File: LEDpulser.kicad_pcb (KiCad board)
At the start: 2 copper layers, 50.7 x 77.8 mm, 70 parts, among them J1 RJHSE-5380, J2 EPS.00.250.NTN, J3 EPS.00.250.NTN, J4 EB21A-04-D, J5 EPL.0S.302.HLN, Q1 BVSS84LT1G, Q2 DMN3028LQ-7, Q3 DMN3028LQ-7, SW1 BST11T2AVR, U1 74AHCT123APW,118, U10 LT3082EST#TRPBF, U2 74AHCT123APW,118, U3 74AHCT123APW,118, U4 SN74LVC2G74, U5 LT1121CST-5#TRPBF, U6 IXDI602SIATR, U7 NE555S-13, U8 PM8834, U9 PM8834

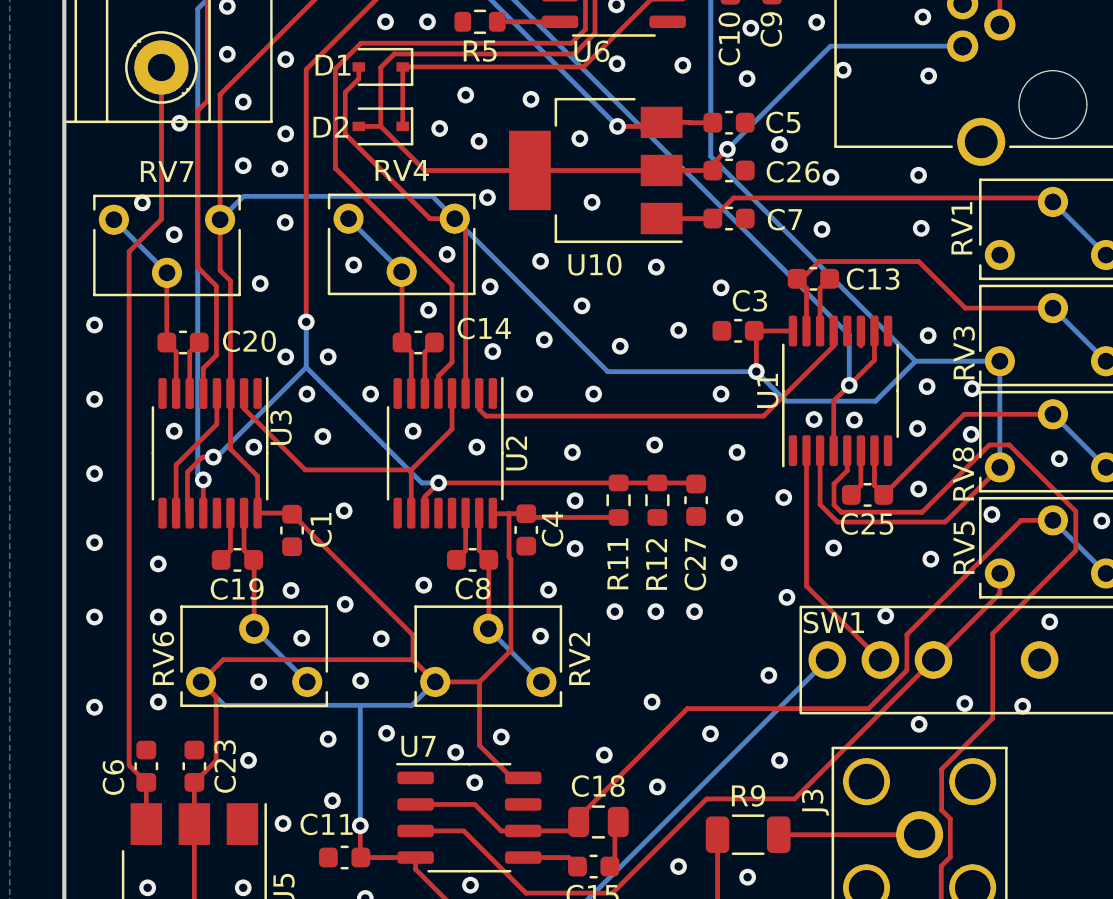
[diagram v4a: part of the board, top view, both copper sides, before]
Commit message: Fixed enable for sync pulse monostable
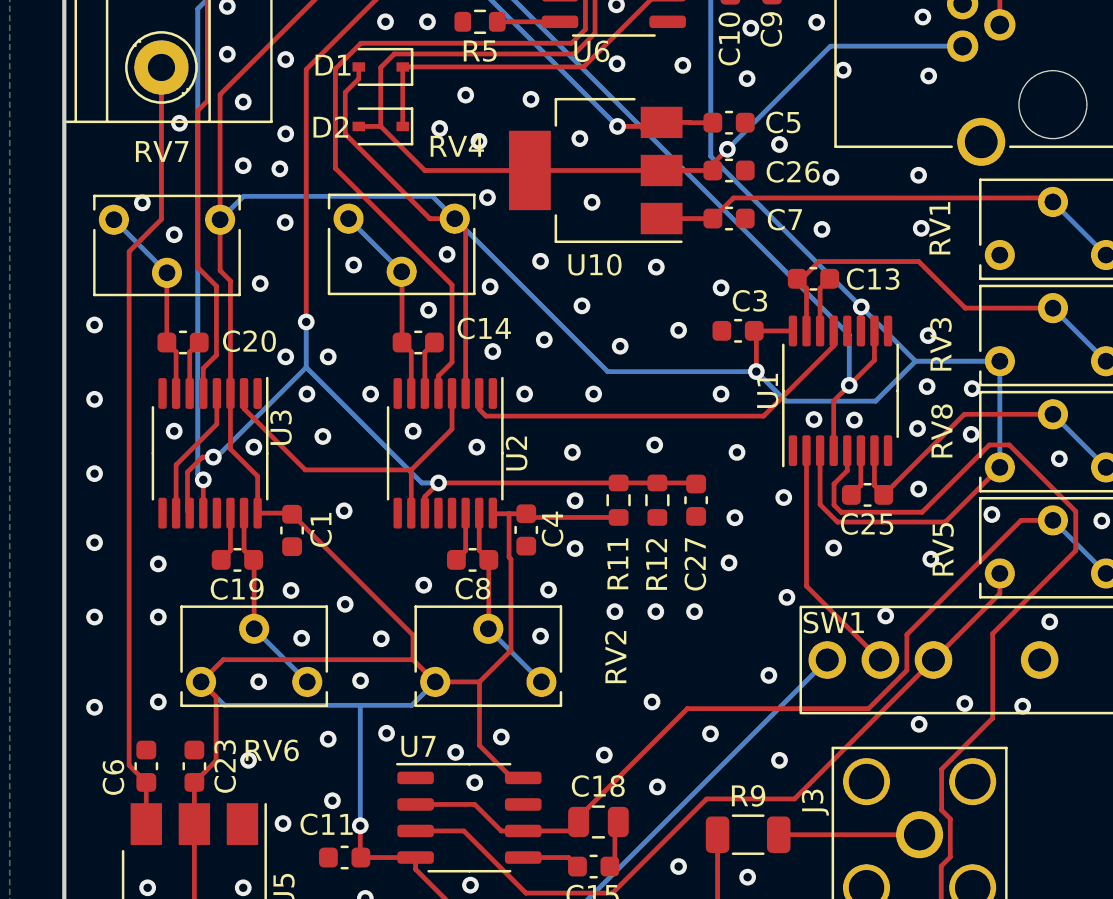
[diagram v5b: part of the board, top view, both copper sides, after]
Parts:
- U5: value LT1121CST-5#TRPBF -> LT1117
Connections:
- U1 pad 11: GND -> VCC
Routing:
- net VCC: track 253.2 -> 254.3 mm, vias 3 -> 4
- net GND: track 24.3 -> 23.6 mm

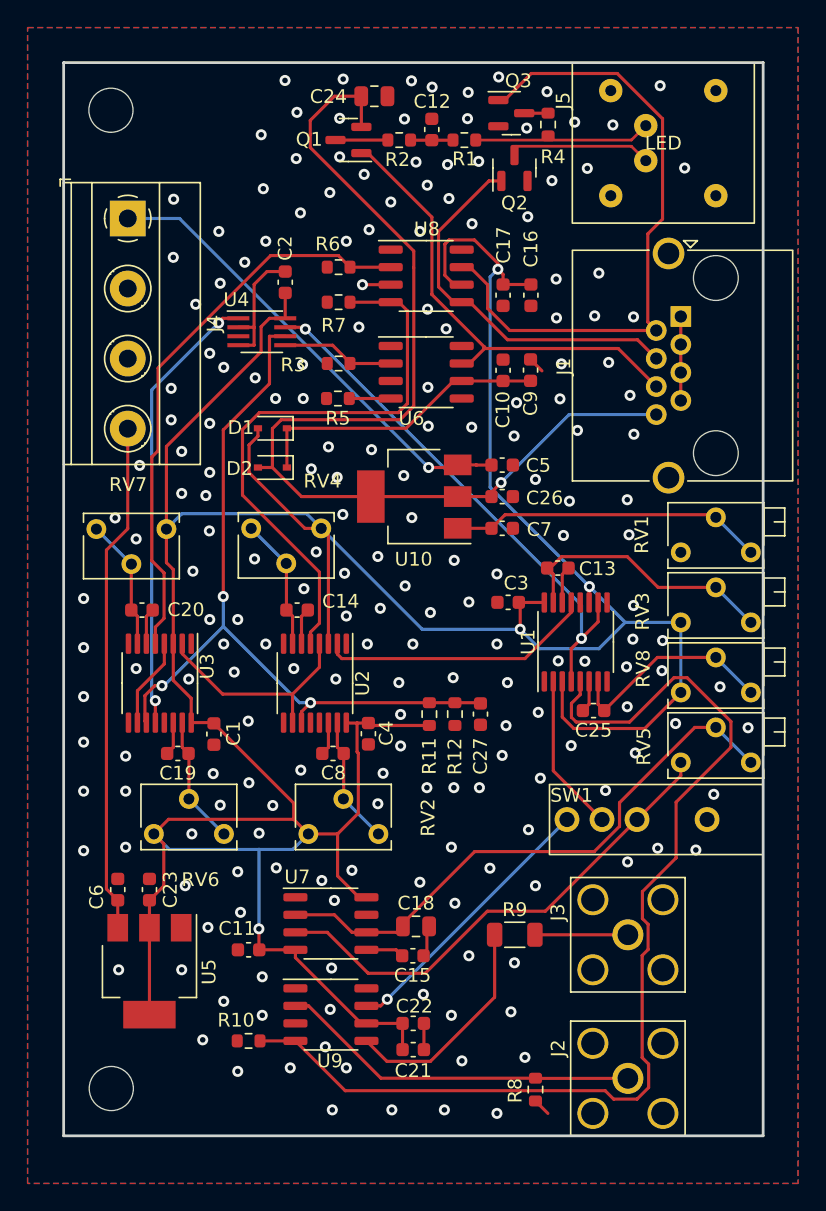
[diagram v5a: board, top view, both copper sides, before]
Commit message: Added third mounting hole. Added cutout for LEMO-connector back-side nuts.
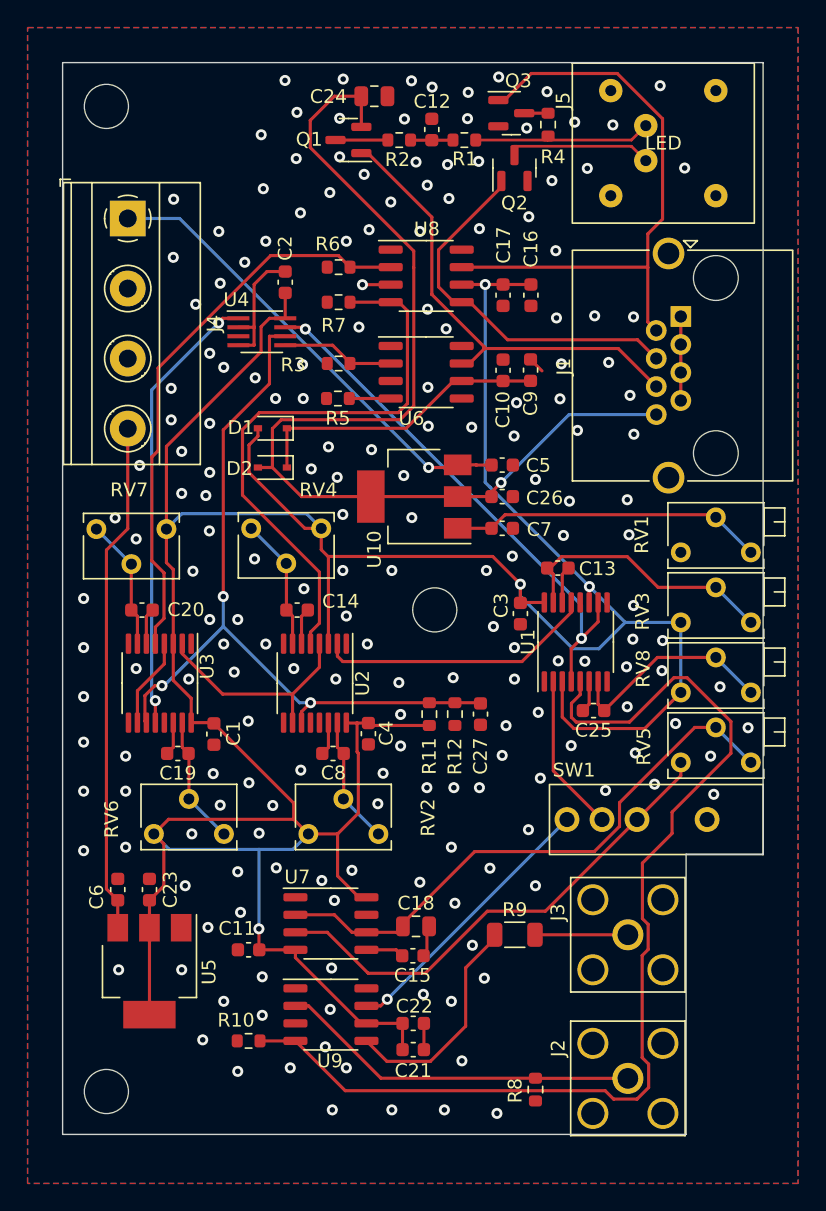
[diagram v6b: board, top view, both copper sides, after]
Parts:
- added H3: MountingHole, MountingHole:MountingHole_3.2mm_M3, F.Cu at (115.9, 65.1)
- moved C3 1.20 mm to (122.1, 65.4), turned to -90 degrees
- moved H1 0.43 mm to (92.1, 28.6)
- moved H2 0.42 mm to (92.1, 100.0)
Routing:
- net VCC: track 254.3 -> 245.2 mm
- net /LED_SHORT_OUT: track 46.1 -> 43.2 mm
- net GND: track 23.6 -> 22.3 mm, vias 203 -> 194
- net /LED_ON_OUT: track 26.9 -> 26.4 mm
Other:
- board size 50.7 x 77.8 mm -> 50.8 x 77.7 mm

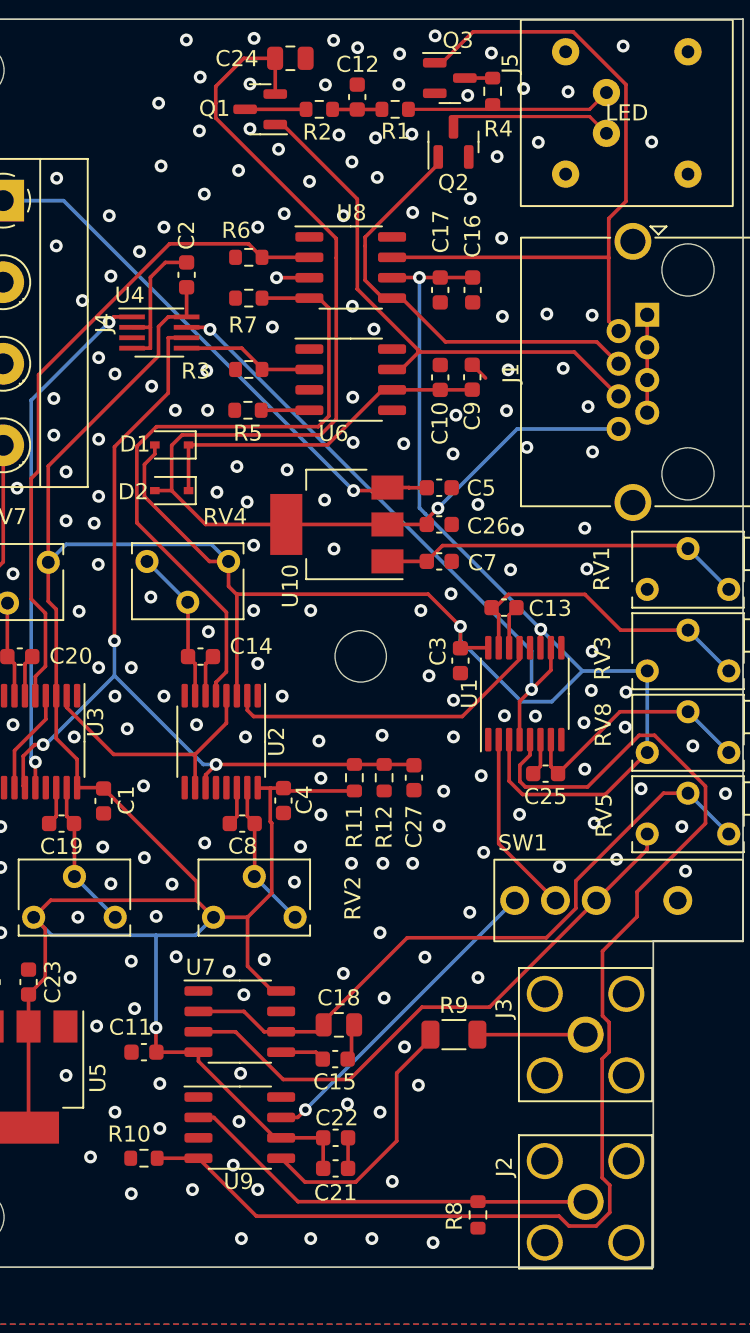
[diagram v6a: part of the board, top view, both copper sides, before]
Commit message: Added labeling to back silk screen
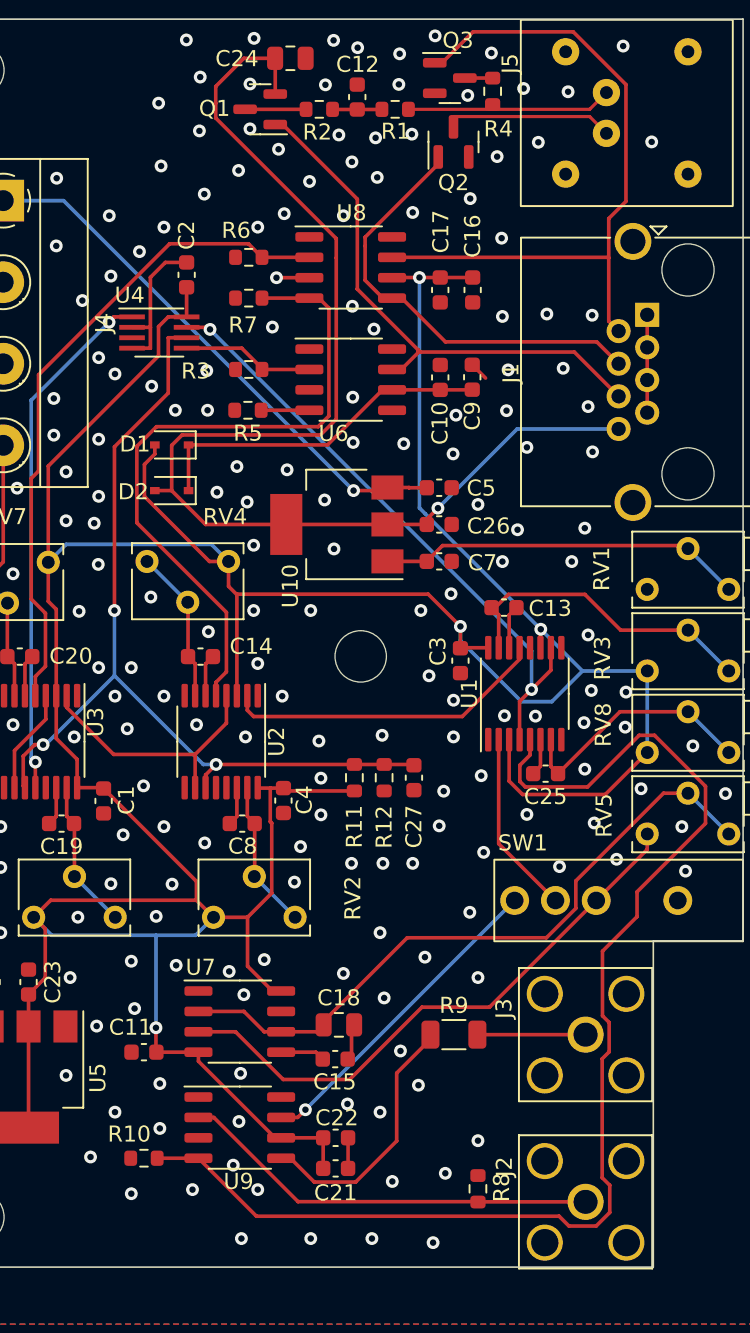
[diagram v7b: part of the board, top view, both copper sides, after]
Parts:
- moved R8 1.63 mm to (123.2, 98.2), turned to 90 degrees
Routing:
- net GND: vias 194 -> 196
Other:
- board text added: "+24V"
- board text added: "+6V"
- board text added: "C12 Charge"
- board text added: "External"
- board text added: "External Trigger In"
- board text added: "GND"
- board text added: "Internal"
- board text added: "LED On"
- board text added: "LED On Delay"
- board text added: "LED On Width"
- board text added: "LED Pulser v2"
- board text added: "LED Short"
- board text added: "LED Short Delay"
- board text added: "LED Short Width"
- board text added: "LED Voltage"
- board text added: "Sync Delay"
- board text added: "Sync Out"
- board text added: "Sync Width"
- board text added: "Trigger Rate Internal"

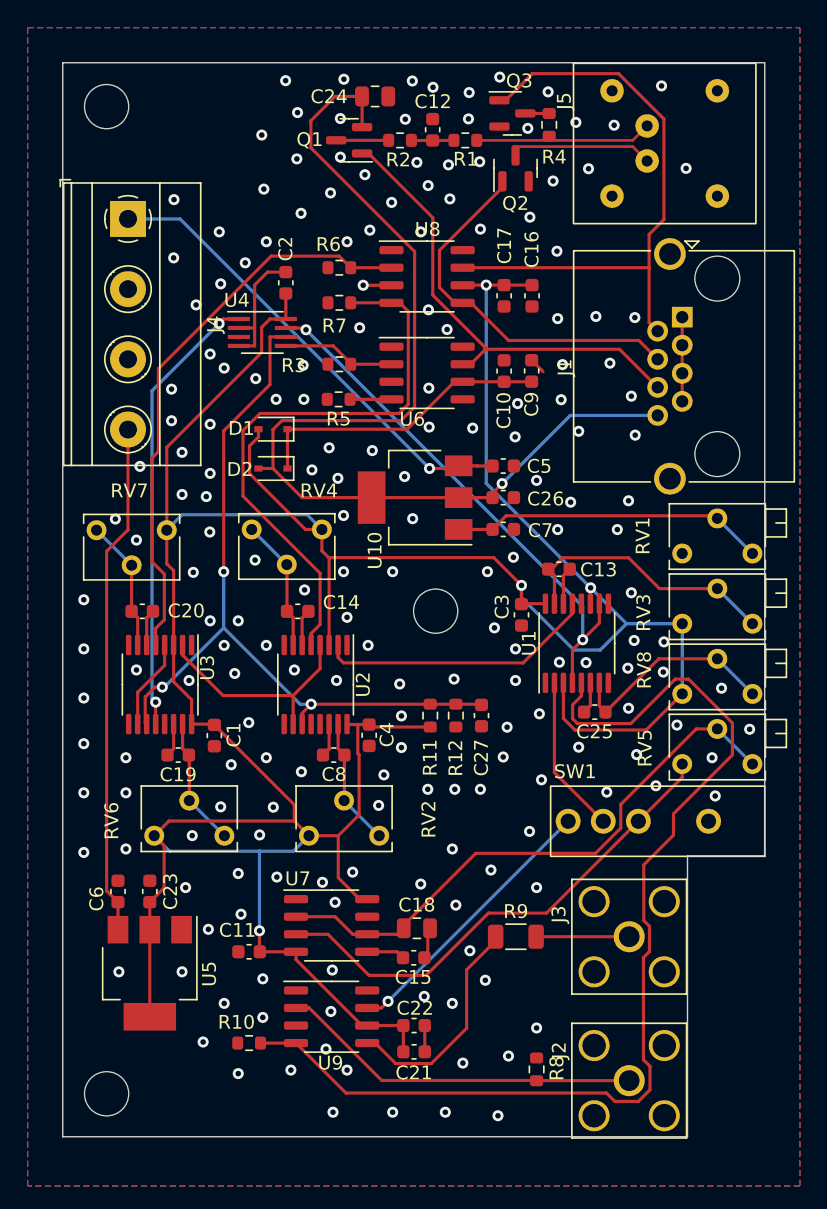
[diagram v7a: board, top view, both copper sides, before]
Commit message: Added series resistors for pots.
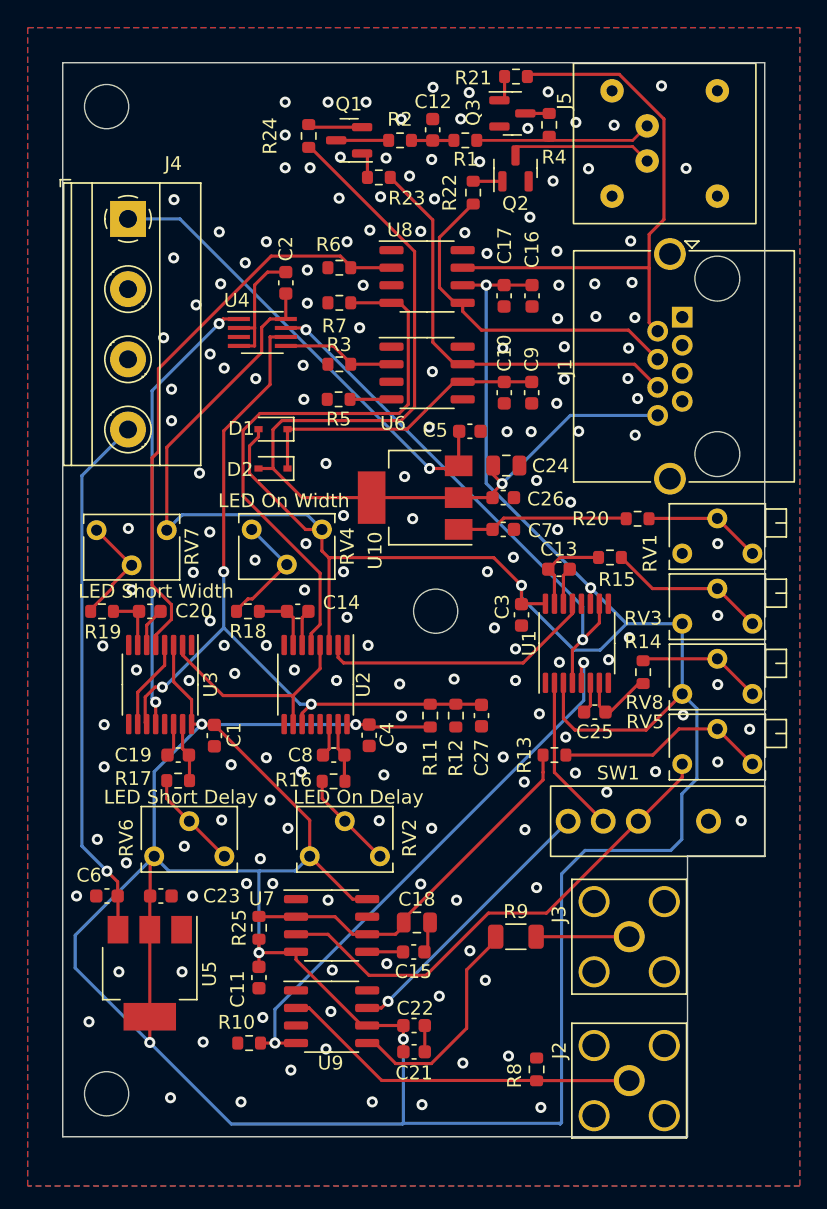
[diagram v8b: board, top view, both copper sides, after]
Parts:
- added R13: 22, Resistor_SMD:R_0603_1608Metric, F.Cu at (124.5, 75.5)
- added R14: 0, Resistor_SMD:R_0603_1608Metric, F.Cu at (130.9, 69.5)
- added R15: 0, Resistor_SMD:R_0603_1608Metric, F.Cu at (128.5, 61.2)
- added R16: 0, Resistor_SMD:R_0603_1608Metric, F.Cu at (108.5, 77.4)
- added R17: 0, Resistor_SMD:R_0603_1608Metric, F.Cu at (97.2, 77.3)
- added R18: 0, Resistor_SMD:R_0603_1608Metric, F.Cu at (102.3, 65.1)
- added R19: 0, Resistor_SMD:R_0603_1608Metric, F.Cu at (91.7, 65.1)
- added R20: 0, Resistor_SMD:R_0603_1608Metric, F.Cu at (130.5, 58.4)
- added R21: 0, Resistor_SMD:R_0603_1608Metric, F.Cu at (121.7, 26.4)
- added R22: 0, Resistor_SMD:R_0603_1608Metric, F.Cu at (118.6, 34.8)
- added R23: 0, Resistor_SMD:R_0603_1608Metric, F.Cu at (111.8, 33.7)
- added R24: 0, Resistor_SMD:R_0603_1608Metric, F.Cu at (106.7, 30.7)
- added R25: DNP, Resistor_SMD:R_0603_1608Metric, F.Cu at (103.1, 88.0)
- Q1: value BVSS84LT1G -> DMP32D4S
- R2: value 1k -> 10k
- RV1: value 2k -> 2Meg
- RV2, RV3: value 500 -> 2k
- moved C24 28.3 mm to (121.0, 54.5)
- moved C5 3.49 mm to (118.4, 52.1)
- moved C11 1.99 mm to (103.1, 91.6), turned to -90 degrees
- moved C9 1.57 mm to (122.8, 49.3), turned to -90 degrees
- moved C10 1.56 mm to (120.8, 49.3), turned to -90 degrees
- moved RV2 1.49 mm to (106.8, 82.8)
- moved RV6 1.49 mm to (95.5, 82.8)
- moved C23 0.87 mm to (96.0, 85.7), turned to 0 degrees
- moved C6 0.86 mm to (92.1, 85.7), turned to 180 degrees
- moved C20 0.54 mm to (95.2, 65.1)
- moved C15 0.42 mm to (114.3, 89.8)
- moved C18 0.42 mm to (114.5, 87.6)
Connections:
- Q1 pad 1: /CAP_CHARGING_OUT -> Net-(Q1-Pad1)
- Q1 pad 2: /CAP_VOLTAGE_OUT -> Net-(Q1-Pad2)
- Q2 pad 1: /LED_ON_OUT -> Net-(Q2-Pad1)
- Q3 pad 1: /LED_SHORT_OUT -> Net-(Q3-Pad1)
- RV1 pad 2: Net-(C7-Pad1) -> Net-(R20-Pad1)
- RV1 pad 3: Net-(C7-Pad1) -> Net-(R20-Pad1)
- RV2 pad 2: Net-(C8-Pad2) -> Net-(R16-Pad1)
- RV2 pad 3: Net-(C8-Pad2) -> Net-(R16-Pad1)
- RV3 pad 2: Net-(C13-Pad1) -> Net-(R15-Pad1)
- RV3 pad 3: Net-(C13-Pad1) -> Net-(R15-Pad1)
- RV4 pad 2: Net-(C14-Pad1) -> Net-(R18-Pad1)
- RV4 pad 3: Net-(C14-Pad1) -> Net-(R18-Pad1)
- RV5 pad 2: Net-(C18-Pad1) -> Net-(R13-Pad1)
- RV5 pad 3: Net-(C18-Pad1) -> Net-(R13-Pad1)
- RV6 pad 2: Net-(C19-Pad1) -> Net-(R17-Pad1)
- RV6 pad 3: Net-(C19-Pad1) -> Net-(R17-Pad1)
- RV7 pad 2: Net-(C20-Pad1) -> Net-(R19-Pad1)
- RV7 pad 3: Net-(C20-Pad1) -> Net-(R19-Pad1)
- RV8 pad 2: Net-(C25-Pad1) -> Net-(R14-Pad2)
- RV8 pad 3: Net-(C25-Pad1) -> Net-(R14-Pad2)
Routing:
- net VCC: track 245.2 -> 335.3 mm, vias 4 -> 8
- net /SYNC: track 77.2 -> 40.9 mm, vias 0 -> 2
- net Net-(R13-Pad1): track 0.00 -> 15.3 mm
- net Net-(C18-Pad1): track 41.7 -> 28.0 mm
- net Net-(C13-Pad1): track 19.6 -> 6.52 mm
- net Net-(R15-Pad1): track 0.00 -> 11.5 mm
- net Net-(C7-Pad1): track 22.5 -> 12.5 mm
- net Net-(C25-Pad1): track 15.6 -> 5.88 mm
- net GND: track 22.3 -> 13.0 mm, vias 196 -> 169
- net Net-(R14-Pad2): track 0.00 -> 9.02 mm
- net Net-(R18-Pad1): track 0.00 -> 8.68 mm
- net Net-(R20-Pad1): track 0.00 -> 8.55 mm
- net Net-(R19-Pad1): track 0.00 -> 8.15 mm
- net Net-(R17-Pad1): track 0.00 -> 7.20 mm
- net Net-(R16-Pad1): track 0.00 -> 7.16 mm
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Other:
- board text added: "Internal Trigger Period"
- board text removed: "Trigger Rate Internal"
